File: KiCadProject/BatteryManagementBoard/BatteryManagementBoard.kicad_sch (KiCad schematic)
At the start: 0 parts

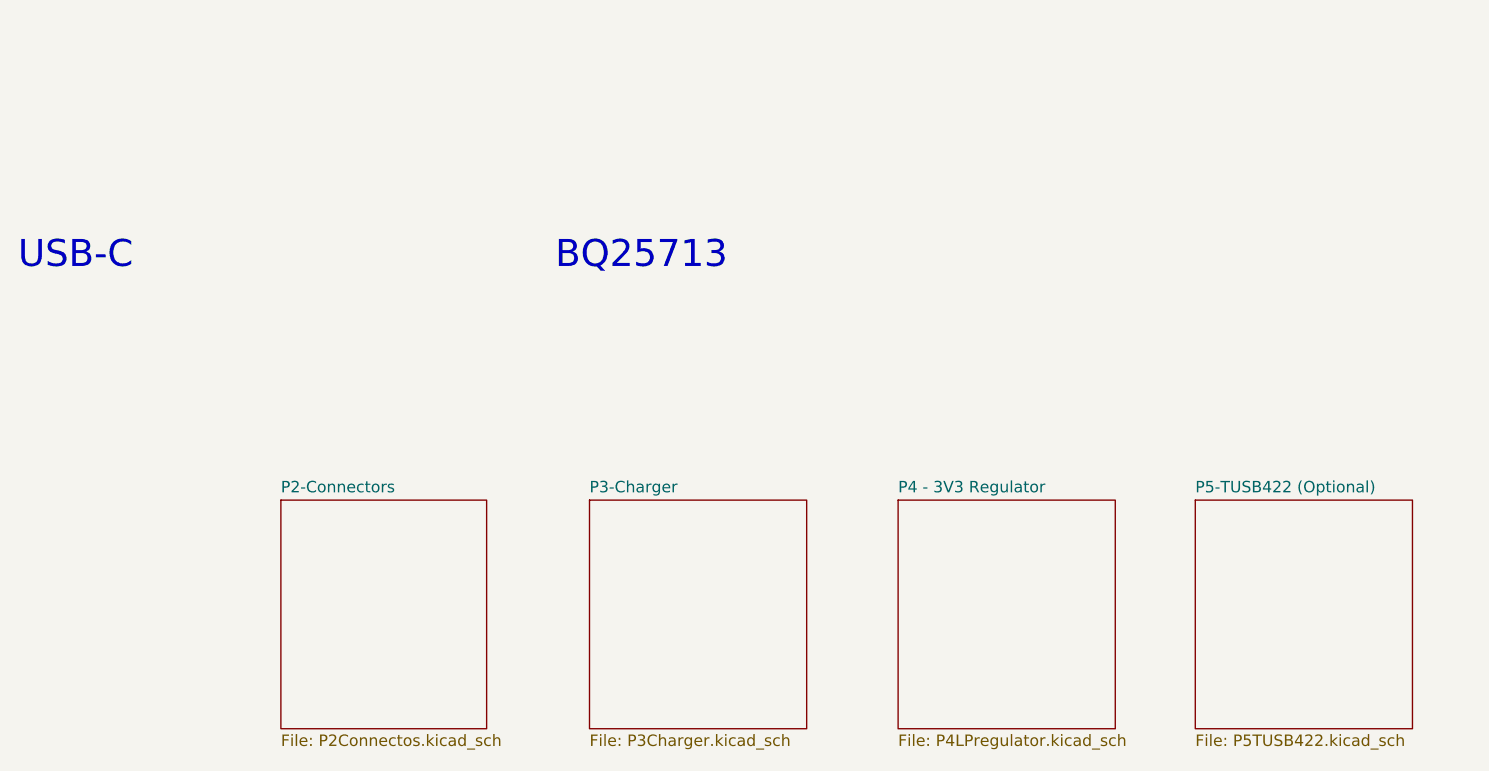
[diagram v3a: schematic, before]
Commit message: All PCB's should be done. Do a final check before ordering.
Signed-off-by: Eldalote.Electronics <Eldalote.Electronics@gmail.com>
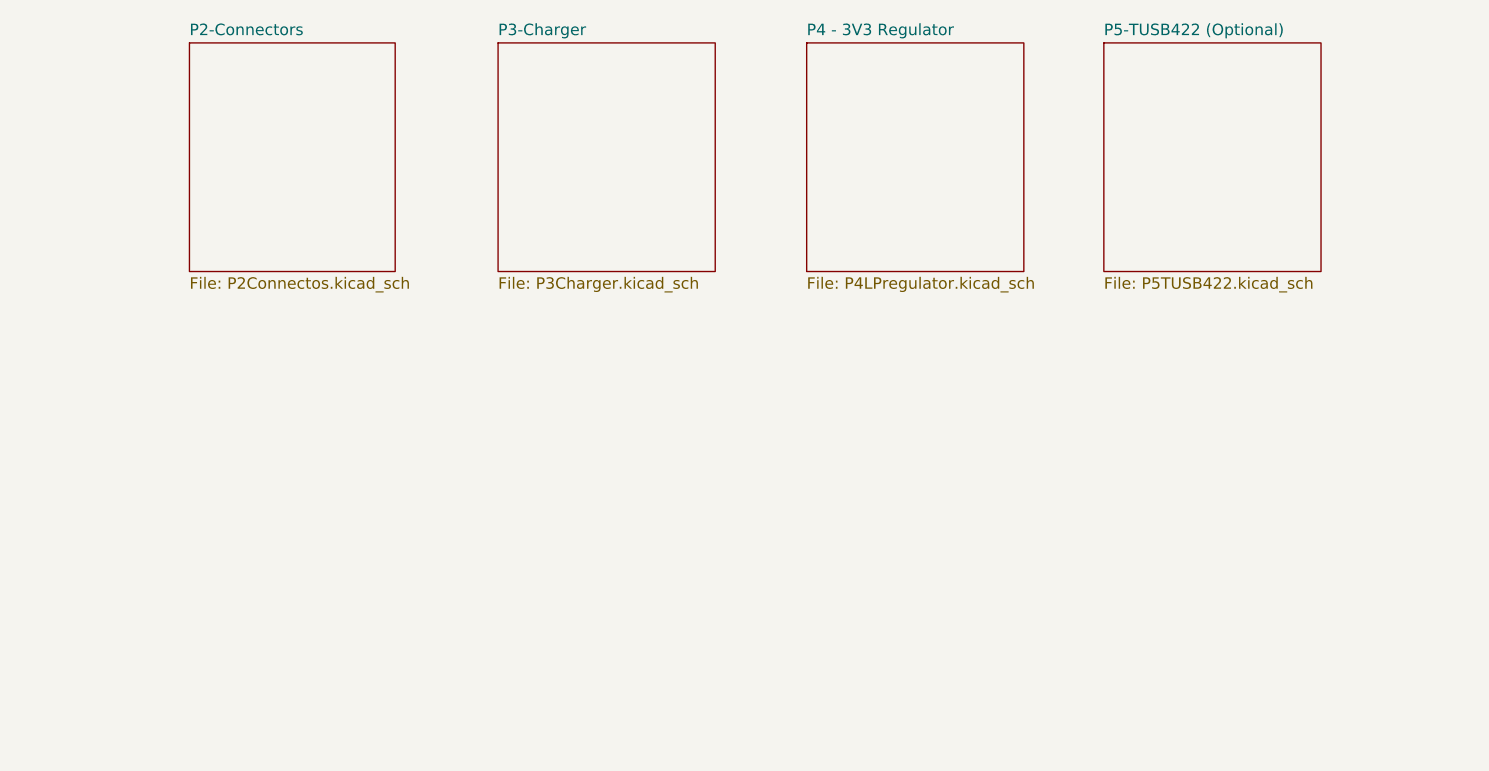
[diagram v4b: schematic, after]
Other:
- note removed: "BQ25713"
- note removed: "USB-C"
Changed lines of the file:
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@@
   (paper "A4")
   (title_block
-    (rev "0.1")
+    (date "2023-02-01")
+    (rev "0.3")
     (company "Eldalote Electronics")
+    (comment 1 "Part of the Dive Lamp design")
     (comment 3 "Battery Charger PCB")
   )
-  (text "USB-C\n" (at 52.07 57.15 0)
-    (effects (font (size 3 3)) (justify left bottom))
-  )
-  (text "BQ25713" (at 111.76 57.15 0)
-    (effects (font (size 3 3)) (justify left bottom))
-  )
-  (sheet (at 182.88 82.55) (size 24.13 25.4) (fields_autoplaced)
+  (sheet (at 172.72 31.75) (size 24.13 25.4) (fields_autoplaced)
     (stroke (width 0.1524) (type solid) (color 0 0 0 0))
     (fill (color 0 0 0 0.0000))
-    (property "Sheet name" "P5-TUSB422 (Optional)" (id 0) (at 182.88 81.8384 0)
+    (property "Sheet name" "P5-TUSB422 (Optional)" (id 0) (at 172.72 31.0384 0)
       (effects (font (size 1.27 1.27)) (justify left bottom))
     )
-    (property "Sheet file" "P5TUSB422.kicad_sch" (id 1) (at 182.88 108.5346 0)
+    (property "Sheet file" "P5TUSB422.kicad_sch" (id 1) (at 172.72 57.7346 0)
       (effects (font (size 1.27 1.27)) (justify left top))
     )
   )
-  (sheet (at 115.57 82.55) (size 24.13 25.4) (fields_autoplaced)
+  (sheet (at 105.41 31.75) (size 24.13 25.4) (fields_autoplaced)
     (stroke (width 0.1524) (type solid) (color 0 0 0 0))
     (fill (color 0 0 0 0.0000))
-    (property "Sheet name" "P3-Charger" (id 0) (at 115.57 81.8384 0)
+    (property "Sheet name" "P3-Charger" (id 0) (at 105.41 31.0384 0)
       (effects (font (size 1.27 1.27)) (justify left bottom))
     )
-    (property "Sheet file" "P3Charger.kicad_sch" (id 1) (at 115.57 108.5346 0)
+    (property "Sheet file" "P3Charger.kicad_sch" (id 1) (at 105.41 57.7346 0)
       (effects (font (size 1.27 1.27)) (justify left top))
     )
   )
-  (sheet (at 149.86 82.55) (size 24.13 25.4) (fields_autoplaced)
+  (sheet (at 139.7 31.75) (size 24.13 25.4) (fields_autoplaced)
     (stroke (width 0.1524) (type solid) (color 0 0 0 0))
     (fill (color 0 0 0 0.0000))
-    (property "Sheet name" "P4 - 3V3 Regulator" (id 0) (at 149.86 81.8384 0)
+    (property "Sheet name" "P4 - 3V3 Regulator" (id 0) (at 139.7 31.0384 0)
       (effects (font (size 1.27 1.27)) (justify left bottom))
     )
-    (property "Sheet file" "P4LPregulator.kicad_sch" (id 1) (at 149.86 108.5346 0)
+    (property "Sheet file" "P4LPregulator.kicad_sch" (id 1) (at 139.7 57.7346 0)
       (effects (font (size 1.27 1.27)) (justify left top))
     )
   )
-  (sheet (at 81.28 82.55) (size 22.86 25.4) (fields_autoplaced)
+  (sheet (at 71.12 31.75) (size 22.86 25.4) (fields_autoplaced)
     (stroke (width 0.1524) (type solid) (color 0 0 0 0))
     (fill (color 0 0 0 0.0000))
-    (property "Sheet name" "P2-Connectors" (id 0) (at 81.28 81.8384 0)
+    (property "Sheet name" "P2-Connectors" (id 0) (at 71.12 31.0384 0)
       (effects (font (size 1.27 1.27)) (justify left bottom))
     )
-    (property "Sheet file" "P2Connectos.kicad_sch" (id 1) (at 81.28 108.5346 0)
+    (property "Sheet file" "P2Connectos.kicad_sch" (id 1) (at 71.12 57.7346 0)
       (effects (font (size 1.27 1.27)) (justify left top))
     )
@@
       (reference "#FLG0201") (unit 1) (value "PWR_FLAG") (footprint "")
     )
-    (path "/69d47876-246e-41ae-905e-9ebbd16344cc/ad9a566d-8ef8-42fe-a66e-a0bfdf813537"
+    (path "/69d47876-246e-41ae-905e-9ebbd16344cc/67e4b76e-c0ce-4f91-8736-5666b5bf456c"
       (reference "#FLG0401") (unit 1) (value "PWR_FLAG") (footprint "")
     )
@@
       (reference "#PWR0107") (unit 1) (value "+3.3V") (footprint "")
     )
+    (path "/6c690547-abab-47ef-b662-94a9d80aa131/16bba7e0-3208-41c4-80e6-fd9a1efd0dd4"
+      (reference "#PWR0108") (unit 1) (value "GND") (footprint "")
+    )
     (path "/6c690547-abab-47ef-b662-94a9d80aa131/23052c76-0aa2-4646-860e-b8b543cdb56f"
       (reference "#PWR0201") (unit 1) (value "GND") (footprint "")
@@
       (reference "#PWR0323") (unit 1) (value "+BATT") (footprint "")
     )
-    (path "/69d47876-246e-41ae-905e-9ebbd16344cc/7f7e97ff-25bb-4015-b764-5a877162e4b4"
+    (path "/69d47876-246e-41ae-905e-9ebbd16344cc/19e6f2d0-b62e-47c7-9e1b-989aa591fa5f"
       (reference "#PWR0401") (unit 1) (value "GND") (footprint "")
     )
-    (path "/69d47876-246e-41ae-905e-9ebbd16344cc/5ae48ea4-e03f-4da6-8932-2110e697ad93"
-      (reference "#PWR0402") (unit 1) (value "+3.3V") (footprint "")
+    (path "/69d47876-246e-41ae-905e-9ebbd16344cc/8c9e8c05-35de-41ea-be93-20dafa66bec2"
+      (reference "#PWR0402") (unit 1) (value "+5V") (footprint "")
+    )
+    (path "/69d47876-246e-41ae-905e-9ebbd16344cc/d15cecea-bffc-4e80-a266-bdb5fcaee24c"
+      (reference "#PWR0403") (unit 1) (value "GND") (footprint "")
+    )
+    (path "/69d47876-246e-41ae-905e-9ebbd16344cc/1865ee0b-aad1-4e7b-9914-e470c8daf62d"
+      (reference "#PWR0404") (unit 1) (value "+3.3V") (footprint "")
     )
     (path "/17028c60-ec89-4f82-89b5-a95e563b4bb5/d59d0527-a350-4bdc-92ac-b2401663c8ec"
@@
       (reference "C333") (unit 1) (value "100p") (footprint "Capacitor_SMD:C_0402_1005Metric")
     )
-    (path "/69d47876-246e-41ae-905e-9ebbd16344cc/6a867d97-793e-4d84-b577-f0a4efe389cd"
-      (reference "C401") (unit 1) (value "22u") (footprint "Capacitor_SMD:CP_Elec_5x5.3")
-    )
-    (path "/69d47876-246e-41ae-905e-9ebbd16344cc/ff5bbe6f-84ff-43fe-a9d5-43bef5f236e7"
-      (reference "C402") (unit 1) (value "100n") (footprint "Capacitor_SMD:C_0402_1005Metric")
-    )
-    (path "/69d47876-246e-41ae-905e-9ebbd16344cc/f648d38f-770a-4049-a706-581e513218ff"
-      (reference "C403") (unit 1) (value "10u") (footprint "Capacitor_SMD:C_0805_2012Metric")
+    (path "/69d47876-246e-41ae-905e-9ebbd16344cc/03291368-323b-4401-ab86-913360ab404d"
+      (reference "C402") (unit 1) (value "10u") (footprint "Capacitor_SMD:C_0805_2012Metric")
+    )
+    (path "/69d47876-246e-41ae-905e-9ebbd16344cc/fb54119b-15f9-4082-9327-9852806cbc0a"
+      (reference "C403") (unit 1) (value "100n") (footprint "Capacitor_SMD:C_0402_1005Metric")
+    )
+    (path "/69d47876-246e-41ae-905e-9ebbd16344cc/e7f01b3b-a9ae-4cee-9afd-10d7d631a83e"
+      (reference "C404") (unit 1) (value "22u") (footprint "Capacitor_SMD:C_0805_2012Metric")
+    )
+    (path "/69d47876-246e-41ae-905e-9ebbd16344cc/9fa3ac84-033c-4810-b3c7-919421603f63"
+      (reference "C405") (unit 1) (value "22u") (footprint "Capacitor_SMD:C_0805_2012Metric")
+    )
+    (path "/69d47876-246e-41ae-905e-9ebbd16344cc/f6be0b8c-8a21-414e-a39b-9577634051af"
+      (reference "C406") (unit 1) (value "10u") (footprint "Capacitor_SMD:C_0805_2012Metric")
+    )
+    (path "/69d47876-246e-41ae-905e-9ebbd16344cc/f47e9320-373c-47fa-be0b-42c984d283dc"
+      (reference "C407") (unit 1) (value "22u") (footprint "Capacitor_SMD:C_0805_2012Metric")
     )
     (path "/17028c60-ec89-4f82-89b5-a95e563b4bb5/e9b8df19-e953-4cb0-8176-87150364598a"
@@
       (reference "J208") (unit 1) (value "JST_B5B_XH") (footprint "Connector_JST:JST_XH_B5B-XH-A_1x05_P2.50mm_Vertical")
     )
+    (path "/6c690547-abab-47ef-b662-94a9d80aa131/31a10c89-0eff-45d2-95aa-a159ebcef15c"
+      (reference "J209") (unit 1) (value "Optional off board USB power connection") (footprint "Connector_PinHeader_2.00mm:PinHeader_1x02_P2.00mm_Vertical")
+    )
+    (path "/6c690547-abab-47ef-b662-94a9d80aa131/a26081ac-49c8-4015-8967-eed9fea5f82e"
+      (reference "J210") (unit 1) (value "Optional off board USB CC connection") (footprint "Connector_PinHeader_1.00mm:PinHeader_1x02_P1.00mm_Vertical")
+    )
     (path "/200fe3a7-2308-4f98-9cee-05cf8e6cdc2a/57f72662-6608-47a4-b0b3-83575f070240"
       (reference "L301") (unit 1) (value "2u2") (footprint "Eldalote-footprints:SRP-1265C")
     )
+    (path "/69d47876-246e-41ae-905e-9ebbd16344cc/23bcddcc-983a-45b2-b3a5-8e14f0665440"
+      (reference "L401") (unit 1) (value "4u7") (footprint "Inductor_SMD:L_1210_3225Metric")
+    )
+    (path "/69d47876-246e-41ae-905e-9ebbd16344cc/289217df-e05b-4913-bd0f-fc41c2790744"
+      (reference "L402") (unit 1) (value "1u") (footprint "Inductor_SMD:L_1210_3225Metric")
+    )
     (path "/200fe3a7-2308-4f98-9cee-05cf8e6cdc2a/0f9eacb6-862e-4eef-858a-e41c67b2ffff"
       (reference "Q301") (unit 1) (value "NFET_Gatenames") (footprint "Eldalote-footprints:DFN3x3A_8L_EP1_P")
@@
       (reference "R506") (unit 1) (value "10k") (footprint "Resistor_SMD:R_0402_1005Metric")
     )
-    (path "/6c690547-abab-47ef-b662-94a9d80aa131/2622fe05-3fff-41e4-a7bf-12e18e5e05cd"
-      (reference "TP201") (unit 1) (value "TestPoint") (footprint "TestPoint:TestPoint_Pad_D1.0mm")
-    )
     (path "/200fe3a7-2308-4f98-9cee-05cf8e6cdc2a/695e3ef7-7b45-45cc-a51b-a40178bf78b6"
       (reference "U301") (unit 1) (value "BQ25713") (footprint "Package_DFN_QFN:Texas_S-PWQFN-N32_EP2.8x2.8mm")
@@
       (reference "U301") (unit 2) (value "BQ25713") (footprint "Package_DFN_QFN:Texas_S-PWQFN-N32_EP2.8x2.8mm")
     )
-    (path "/69d47876-246e-41ae-905e-9ebbd16344cc/38e94db3-ee79-4c05-82ab-aca1d01efb6e"
-      (reference "U401") (unit 1) (value "BD433M5FP") (footprint "Package_TO_SOT_SMD:TO-252-3_TabPin4")
+    (path "/69d47876-246e-41ae-905e-9ebbd16344cc/aaf654d6-9879-4986-af77-e4cb1efdc11c"
+      (reference "U401") (unit 1) (value "AP63205WU") (footprint "Package_TO_SOT_SMD:TSOT-23-6")
+    )
+    (path "/69d47876-246e-41ae-905e-9ebbd16344cc/922291ee-8081-459e-8460-abf931096788"
+      (reference "U402") (unit 1) (value "SC189") (footprint "Package_TO_SOT_SMD:SOT-23-5")
     )
     (path "/17028c60-ec89-4f82-89b5-a95e563b4bb5/d3620ca1-0949-4735-8de9-a05125d99fa7"

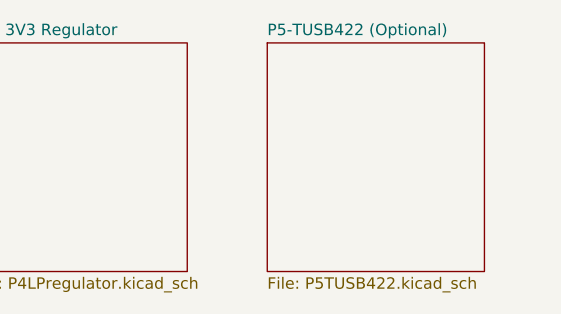
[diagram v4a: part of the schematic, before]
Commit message: Made ready to order PCBs. Some problems with ordering due to misunderstanding. Thinking about solutions
Signed-off-by: Eldalote.Electronics <Eldalote.Electronics@gmail.com>
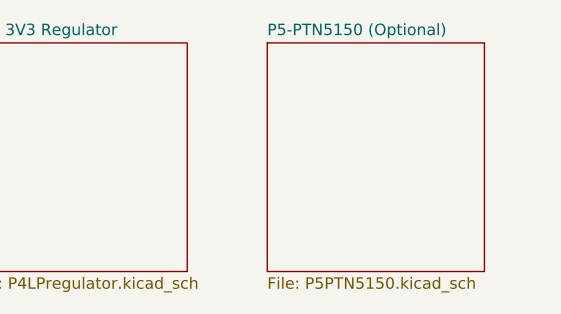
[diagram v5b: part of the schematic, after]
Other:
- sheet P5-TUSB422 (Optional) renamed P5-PTN5150 (Optional)
- sheet P5-PTN5150 (Optional): file P5TUSB422.kicad_sch -> P5PTN5150.kicad_sch
